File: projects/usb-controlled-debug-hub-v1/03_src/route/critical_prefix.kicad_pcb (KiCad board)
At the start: 4 copper layers, 130 x 90 mm, 146 parts

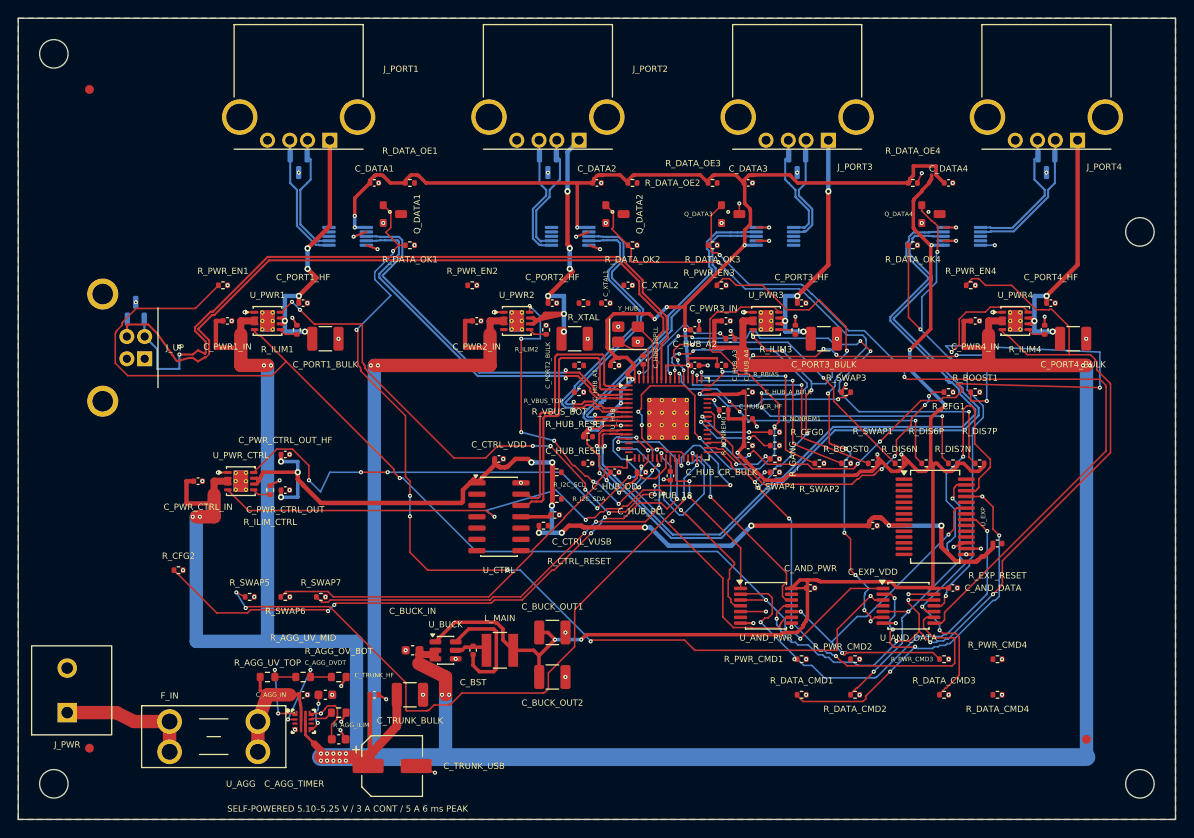
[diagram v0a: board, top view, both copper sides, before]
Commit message: Complete debug hub routing and release gates
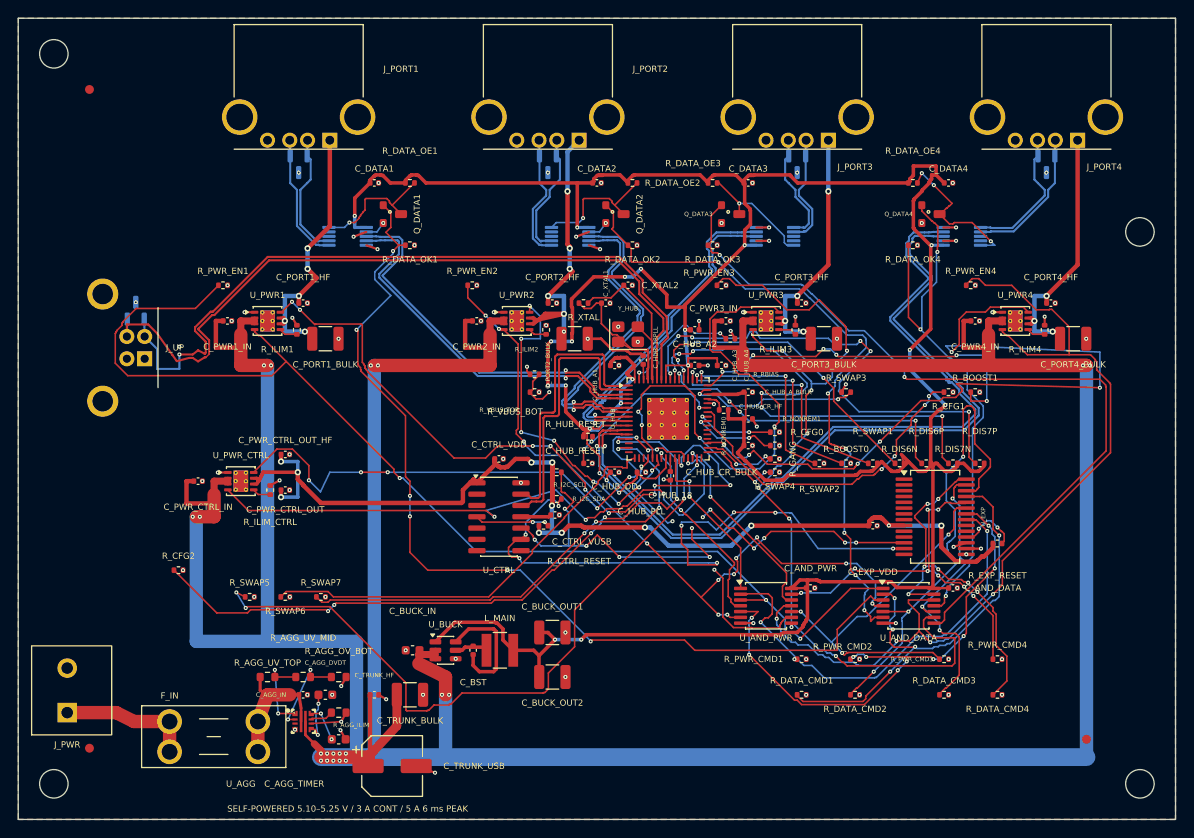
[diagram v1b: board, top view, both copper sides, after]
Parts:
- moved R_VBUS_TOP 5.10 mm to (78.0, 60.0)
- moved R_VBUS_BOT 5.00 mm to (78.0, 62.0)
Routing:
- net PWR_EN2: track 0.00 -> 82.8 mm, vias 0 -> 12
- net I2C_SDA: track 0.00 -> 71.4 mm, vias 0 -> 8
- net I2C_SCL: track 0.00 -> 65.3 mm, vias 0 -> 12
- net USB_UP_VBUS: track 0.00 -> 59.6 mm, vias 0 -> 1
- net PWR_CMD2: track 2.86 -> 61.1 mm, vias 1 -> 10
- net PWR_CMD4: track 0.00 -> 42.7 mm, vias 0 -> 8
- net DATA_CMD4: track 2.86 -> 41.2 mm, vias 1 -> 7
- net HUB_VBUS_SENSE: track 0.00 -> 28.5 mm, vias 0 -> 2
- net 3V3_MAIN: track 363.4 -> 384.8 mm, vias 23 -> 22
- net HUB_RESET_N: track 0.00 -> 19.5 mm, vias 0 -> 3
- net GND: track 40.1 -> 57.9 mm, vias 116 -> 117
- net XTAL2: track 6.62 -> 23.4 mm
- net XTAL1: track 6.95 -> 22.0 mm
- net DATA_OE2_N: track 0.00 -> 15.0 mm, vias 0 -> 1
- net DATA_OE1_N: track 0.00 -> 14.6 mm, vias 0 -> 1
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
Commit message: fix USB debug hub power sense and connector orientation
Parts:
- R_VBUS_TOP: value 100kΩ -> 47kΩ
- moved J_PWR 5.50 mm to (25.5, 92.5), turned to -90 degrees
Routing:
- net HUB_RESET_N: track 19.5 -> 28.4 mm
- net P5V_RAW: track 15.1 -> 20.2 mm
- net GND: track 57.9 -> 59.9 mm
- net HUB_VBUS_SENSE: track 28.5 -> 29.1 mm
- added copper zone on F.Cu, net P5V_FUSED
- added copper zone on B.Cu, net P5V_PROTECTED
- added copper zone on F.Cu, net P5V_PROTECTED
- added copper zone on F.Cu, net P5V_RAW
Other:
- board text added: "+5V"
- board text added: "4A FUSE"
- board text added: "5V INPUT"
- board text added: "GND"
- board text added: "PORT 1"
- board text added: "PORT 2"
- board text added: "PORT 3"
- board text added: "PORT 4"
- board text added: "UPSTREAM USB"
